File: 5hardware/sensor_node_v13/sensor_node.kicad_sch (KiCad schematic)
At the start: 38 parts, among them J1 Conn_01x08_Socket, J2 Conn_01x08_Socket, Q2 AO3401A, Q3 MMBT5551L, Q4 AO3401A, SW1 SW_Push, SW2 SW_Push, SW3 SW_Push, SW4 SW_Reed, SW5 SW_Push, SW6 SW_Push, SW7 SW_Push, U1 ESP-12F, U12 APDS-9960, U13 SHT31-DIS, U17 BH1750FVI-TR, U2 2N7002DW, U7 XC6206PxxxMR, U8 TPL5110

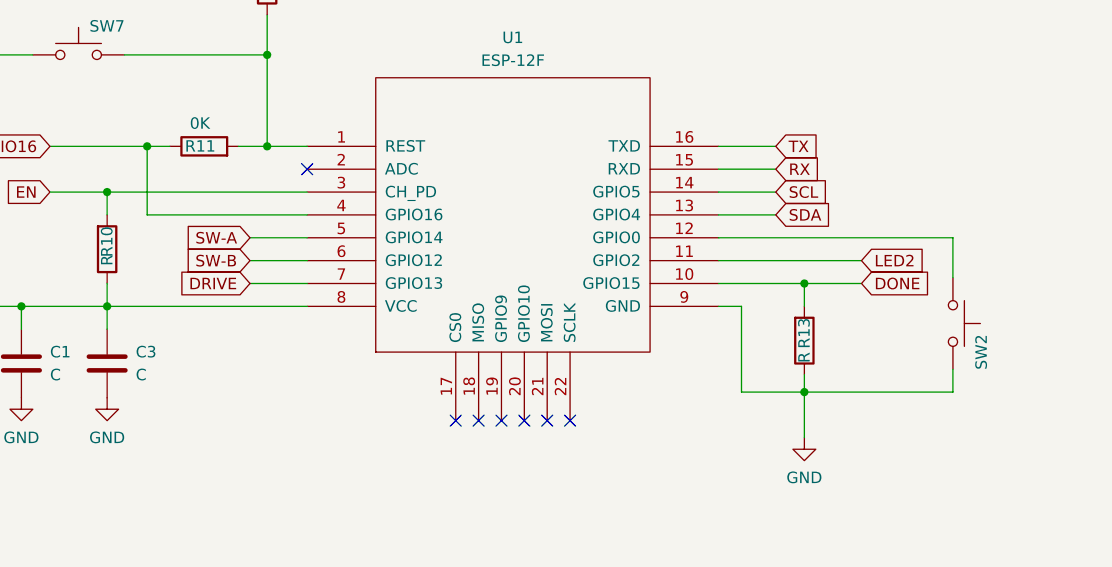
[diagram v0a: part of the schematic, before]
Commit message: update EspNow sensor.
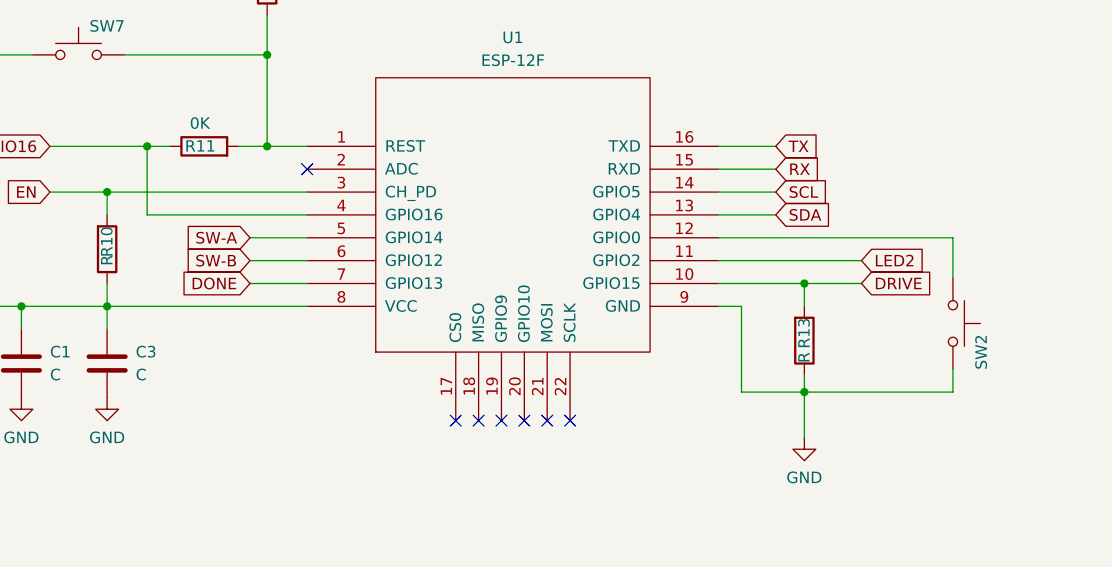
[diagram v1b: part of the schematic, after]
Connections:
- net DONE: now also U1.7 (GPIO13); no longer R13.2, U1.10 (GPIO15)
- net DRIVE: now also R13.2, U1.10 (GPIO15); no longer U1.7 (GPIO13)
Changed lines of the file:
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@@
     )
   )
-  (global_label "DRIVE" (shape input) (at 278.13 172.72 180) (fields_autoplaced)
+  (global_label "DONE" (shape input) (at 278.13 172.72 180) (fields_autoplaced)
     (effects (font (size 1.27 1.27)) (justify right))
-    (property "Intersheetrefs" "${INTERSHEET_REFS}" (at 269.7624 172.72 0)
+    (property "Intersheetrefs" "${INTERSHEET_REFS}" (at 270.0648 172.72 0)
       (effects (font (size 1.27 1.27)) (justify right) hide)
     )
   )
-  (global_label "DONE" (shape input) (at 346.075 172.72 0) (fields_autoplaced)
+  (global_label "DRIVE" (shape input) (at 346.075 172.72 0) (fields_autoplaced)
     (effects (font (size 1.27 1.27)) (justify left))
-    (property "Intersheetrefs" "${INTERSHEET_REFS}" (at 354.1402 172.72 0)
+    (property "Intersheetrefs" "${INTERSHEET_REFS}" (at 354.4426 172.72 0)
       (effects (font (size 1.27 1.27)) (justify left) hide)
     )

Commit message: cleanup.
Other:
- moved on the sheet: C1, C3, R10, R11, R13, R4, R9, SW2, SW7, U1

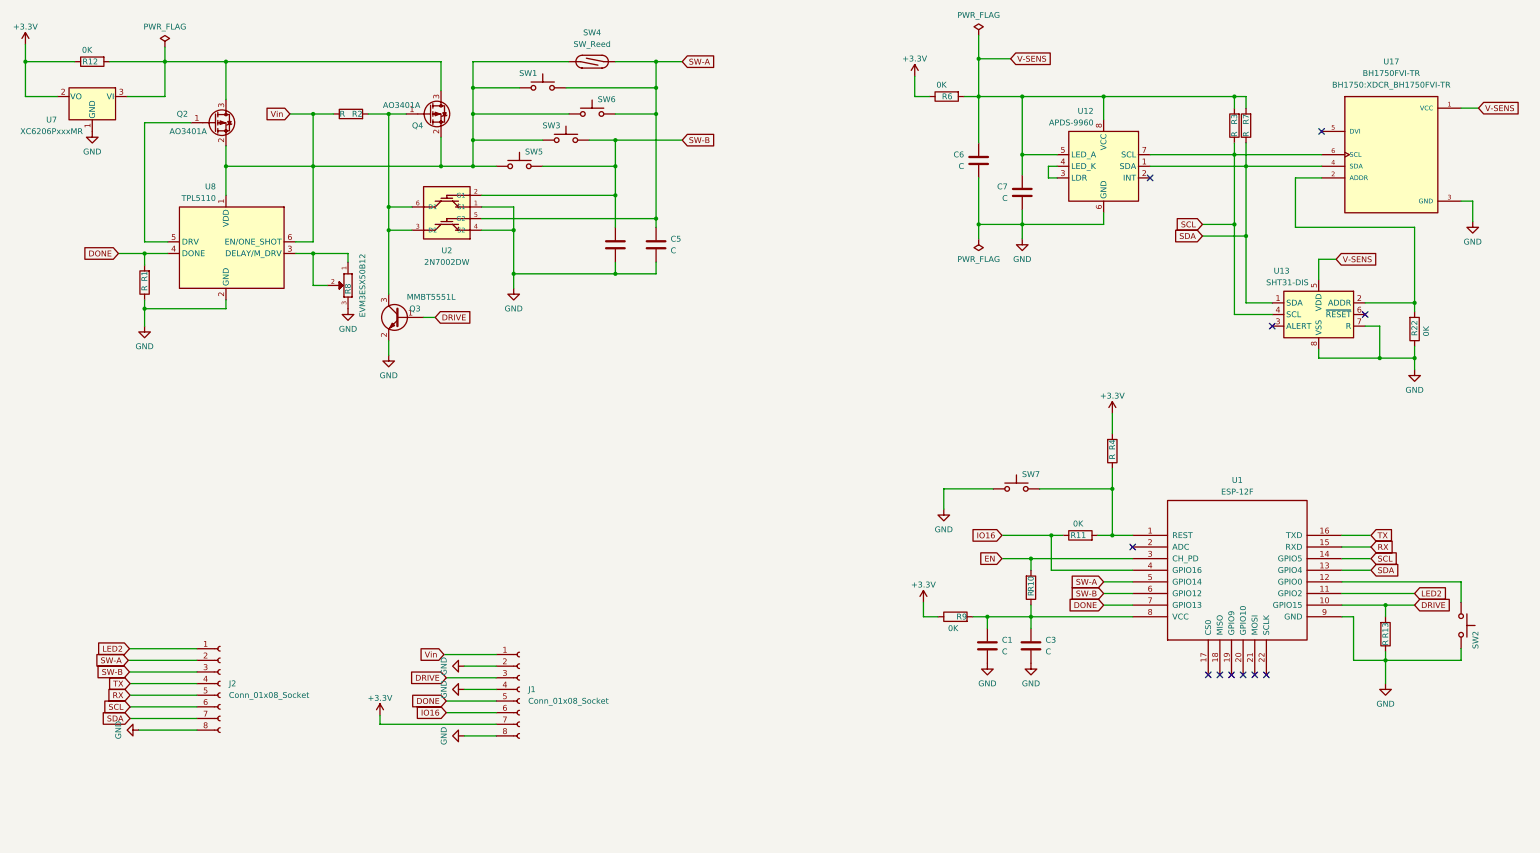
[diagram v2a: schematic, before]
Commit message: update schematic.
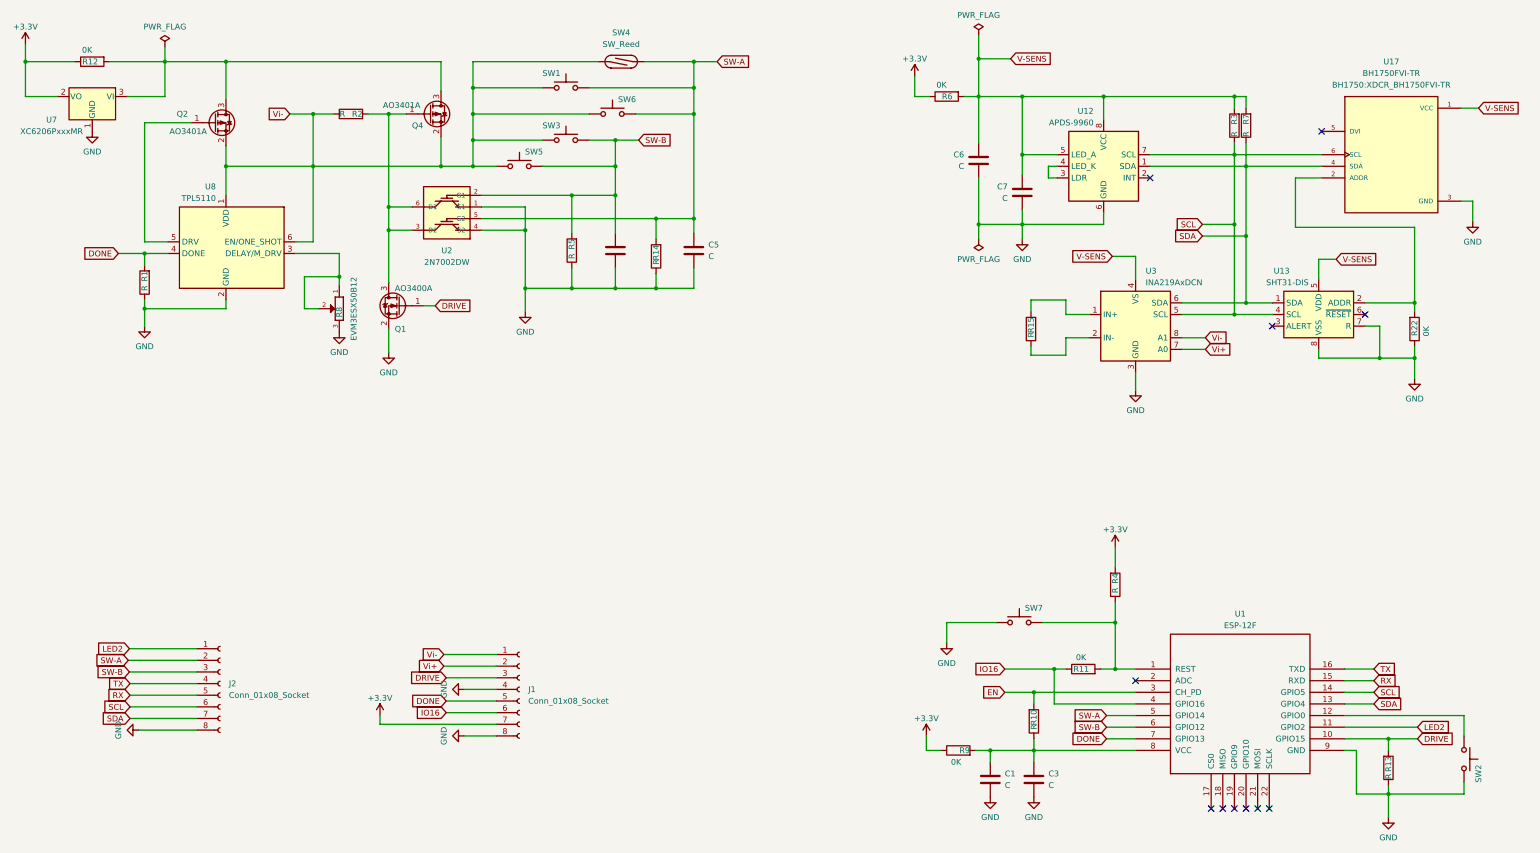
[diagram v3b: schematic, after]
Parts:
- removed Q3: MMBT5551L, Package_TO_SOT_SMD:SOT-23, symbol Transistor_BJT:MMBT5551L
- added Q1: AO3400A, Package_TO_SOT_SMD:SOT-23, symbol Transistor_FET:AO3400A
- added R14, R5: R, Resistor_SMD:R_0603_1608Metric, symbol Device:R
- added R15: R, Resistor_SMD:R_2512_6332Metric, symbol Device:R
- added U3: INA219AxDCN, Package_TO_SOT_SMD:SOT-23-8, symbol Sensor_Energy:INA219AxDCN
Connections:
- net DRIVE: now also Q1.1 (G)
- net GND: now also Q1.2 (S), R14.1, R5.1, U3.3 (GND); no longer J1.2 (Pin_2)
- net SCL: now also U3.5 (SCL)
- net SDA: now also U3.6 (SDA)
- net SW-A: now also R14.2
- net SW-B: now also R5.2
- net V-SENS: now also U3.4 (VS)
- net at Q4.1 (G), R2.2, U2.3 (D2)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: now also Q1.3 (D)
- net Vin renamed Vi-
- net Vi-: now also U3.8 (A1)
- new net: R15.2, U3.1 (IN+)
- new net: R15.1, U3.2 (IN-)
- new net Vi+: J1.2 (Pin_2), U3.7 (A0)
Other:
- moved on the sheet: C1, C3, C5, R10, R11, R13, R4, R8, R9, SW1, SW2, SW4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

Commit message: updated PCB.
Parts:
- removed J1: Conn_01x08_Socket, Connector_PinSocket_2.54mm:PinSocket_1x08_P2.54mm_Vertical, symbol Connector:Conn_01x08_Socket
- removed R8: EVM3ESX50B12, EVM3ES:EMV3ESX50B12, symbol EVM3ESX50B:EVM3ESX50B12
- removed SW4: SW_Reed, Button_Switch_SMD:SW_SPST_REED_CT10-XXXX-G1, symbol Switch:SW_Reed
- removed SW5, SW6: SW_Push, Button_Switch_SMD:SW_SPST_PTS810, symbol Switch:SW_Push
- added J3: Conn_01x09_Socket, Connector_PinSocket_2.54mm:PinSocket_1x09_P2.54mm_Vertical, symbol Connector:Conn_01x09_Socket
- added R16, R19, R20: 0K, Resistor_SMD:R_0402_1005Metric, symbol Device:R
- added R17, R18, R8: R, Resistor_SMD:R_0603_1608Metric, symbol Device:R
- R11, R12, R6, R9: footprint Resistor_SMD:R_0603_1608Metric -> Resistor_SMD:R_0402_1005Metric
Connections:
- net +3.3V: now also J3.9 (Pin_9)
- net DONE: now also J3.5 (Pin_5)
- net DRIVE: now also J3.3 (Pin_3)
- net GND: now also J2.6 (Pin_6), J3.4 (Pin_4), R19.1, R20.1, R8.1; no longer J2.8 (Pin_8)
- net IO16: now also J3.6 (Pin_6)
- net SCL: now also J2.7 (Pin_7); no longer J2.6 (Pin_6)
- net SDA: now also J2.8 (Pin_8); no longer J2.7 (Pin_7)
- net Vi+: now also J3.1 (Pin_1)
- net Vi-: now also J3.2 (Pin_2), R16.1; no longer Q2.2 (S), Q4.2 (S), R2.1, SW1.1, SW3.1, U8.1 (VDD), U8.6 (EN/ONE_SHOT)
- net at U8.3 (DELAY/M_DRV): now also R17.2, R18.2, R8.2
- net S1: now reaches Q2.3 (D), Q4.3 (D), R12.2, U7.3 (VI)
- net S1: now also J3.8 (Pin_8)
- new net: R18.1, R19.2
- new net: R17.1, R20.2
- new net S2: J3.7 (Pin_7), Q2.2 (S), Q4.2 (S), R16.2, R2.1, SW1.1, SW3.1, U8.1 (VDD), U8.6 (EN/ONE_SHOT)
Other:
- moved on the sheet: SW1, SW3
